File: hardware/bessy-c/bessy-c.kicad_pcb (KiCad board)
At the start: 2 copper layers, 91.5 x 134.5 mm, 55 parts, among them J1 rotary_encoder, J10 fan, J11 auger, J2 probe0, J3 probe1, J4 probe2, J5 PTD, J6 igniter, J7 Display, J8 fire_pit, J9 line_in, K1 1462042-7, K2 1462042-7, K3 1462042-7, Q1 BC847, Q2 SCS-1002K, Q3 BC847, Q4 BC847, U1 ProS3, U2 ADS1115IDGS, U3 MCP96xx01x-x-MX, U4 IRM-10-5, U5 NAU7802SGI

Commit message: Ordered bessy-c pcba rev 1
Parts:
- removed Q2: SCS-1002K, Digikey_SCS_1002K:TRAN_SCS-1002K_SIG
- added C8: 10uF, Capacitor_SMD:C_0805_2012Metric, F.Cu at (94.9, 112.8)
- added D1: 1N4148W, Diode_SMD:D_SOD-123, F.Cu at (124.3, 122.7)
- added D2: 1N4148W, Diode_SMD:D_SOD-123, F.Cu at (116.8, 122.7)
- added D3: 1N4148W, Diode_SMD:D_SOD-123, F.Cu at (106.9, 122.7)
- added D4: BZT52C24, Diode_SMD:D_SOD-123F, F.Cu at (129.4, 122.7)
- added R22: 10k, Resistor_SMD:R_0805_2012Metric, F.Cu at (90.9, 112.8)
- added T1: ZMCT102, kicad-jcl-lib:XFMR_ZMCT102, F.Cu at (93.2, 130.0)
- added U6: ADS1115IDGS, Package_SO:TSSOP-10_3x3mm_P0.5mm, F.Cu at (91.9, 117.6)
- C5, C6, C7: value .1uF -> 0.1uF
- J1: value rotary_encoder -> Conn_01x05; footprint TerminalBlock:TerminalBlock_MaiXu_MX126-5.0-05P_1x05_P5.00mm -> Connector_PinHeader_2.54mm:PinHeader_1x05_P2.54mm_Vertical
- J10: value fan -> DB300V-5.0-2P-BK-S
- J11: value auger -> DB300V-5.0-2P-BK-S
- J2: value probe0 -> DB300V-5.0-2P-BK-S
- J3: value probe1 -> DB300V-5.0-2P-BK-S
- J4: value probe2 -> DB300V-5.0-2P-BK-S
- J5: value PTD -> DB300V-5.0-2P-BK-S
- J6: value igniter -> DB300V-5.0-2P-BK-S
- J7: value Display -> Conn_01x14; footprint Connector_PinHeader_2.54mm:PinHeader_1x15_P2.54mm_Vertical -> Connector_PinHeader_2.54mm:PinHeader_1x14_P2.54mm_Vertical
- J8: value fire_pit -> DB300V-5.0-2P-BK-S
- J9: value line_in -> DB300V-5.0-2P-BK-S
- K1, K2, K3: value 1462042-7 -> G5NB; footprint Digikey_1462042_7_Relay:IM-C_THRU_TEC -> Relay_THT:Relay_SPST_Omron_G5NB
- Q1, Q3, Q4: value BC847 -> MMBT2222A
- R19: value 3k -> 3.3k
- U3: value MCP96xx01x-x-MX -> MCP96L00T-E/MX
- moved J7 71.6 mm to (60.5, 57.1), turned to 0 degrees
- moved R3 33.5 mm to (93.6, 50.0)
- moved J1 33.4 mm to (111.5, 46.0), turned to -90 degrees
- moved R1 33.1 mm to (97.8, 55.0), turned to -90 degrees
- moved C2 32.2 mm to (93.0, 55.0)
- moved R2 30.3 mm to (97.8, 59.0), turned to -90 degrees
- moved C1 29.5 mm to (93.0, 59.0)
- moved R4 27.4 mm to (110.6, 63.2), turned to 180 degrees
- moved J2 25.0 mm to (126.0, 60.2)
- moved J3 25.0 mm to (126.0, 74.2)
- moved J4 25.0 mm to (126.0, 88.2)
- moved J5 25.0 mm to (126.0, 101.7)
- moved J8 25.0 mm to (126.0, 115.2)
- moved U2 24.9 mm to (106.2, 68.1)
- moved R7 23.2 mm to (106.3, 63.2), turned to 0 degrees
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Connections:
- Q1 pad 3: Net-(Q1-C) -> Net-(D3-A)
- Q3 pad 3: Net-(Q3-C) -> Net-(D2-A)
- Q4 pad 3: Net-(Q4-C) -> Net-(D1-A)
- R10 pad 1: GND -> Net-(U6-AIN3)
- R10 pad 2: /igniter_current -> Net-(U6-AIN2)
- U1 pad 16: /tft_cs -> unconnected-(U1-IO13-Pad16)
- U1 pad 17: /tft_dc -> unconnected-(U1-IO12-Pad17)
- U1 pad 18: /IO42 -> /auger
- U1 pad 19: /auger -> /fan
- U1 pad 20: /fan -> /igniter
- U1 pad 21: /igniter -> /tft_cs
- U1 pad 22: /IO38 -> /tft_rst
- U1 pad 23: /IO44 -> /tft_dc
- U2 pad 7: /igniter_current -> unconnected-(U2-AIN3-Pad7)
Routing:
- net /igniter_current: track 69.8 -> 0.00 mm
- net /tft_dc: track 61.0 -> 8.12 mm, vias 2 -> 0
- net +3.3V: track 237.6 -> 187.9 mm, vias 4 -> 10
- net /tft_cs: track 57.3 -> 8.51 mm, vias 2 -> 0
- net /enc_b: track 52.6 -> 12.0 mm
- net Net-(J5-Pin_1): track 53.6 -> 14.1 mm, vias 1 -> 0
- net /spi_miso: track 65.8 -> 28.6 mm, vias 1 -> 0
- net Net-(U5-AVDD/LDO): track 22.7 -> 59.0 mm
- net /enc_a: track 47.3 -> 12.6 mm
- net +5V: track 155.5 -> 189.5 mm
- net Net-(J8-Pin_1): track 44.1 -> 11.7 mm
- net /spi_clk: track 64.2 -> 32.5 mm, vias 2 -> 0
- net /spi_mosi: track 60.5 -> 29.2 mm, vias 2 -> 0
- net Net-(J5-Pin_2): track 37.4 -> 8.92 mm, vias 1 -> 0
- net Net-(Q1-C): track 28.5 -> 0.00 mm, vias 1 -> 0
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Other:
- board size 91.5 x 134.5 mm -> 77.5 x 118 mm
- board text added: "JLCJLCJLCJLC"
- board text removed: "Main Sheet"

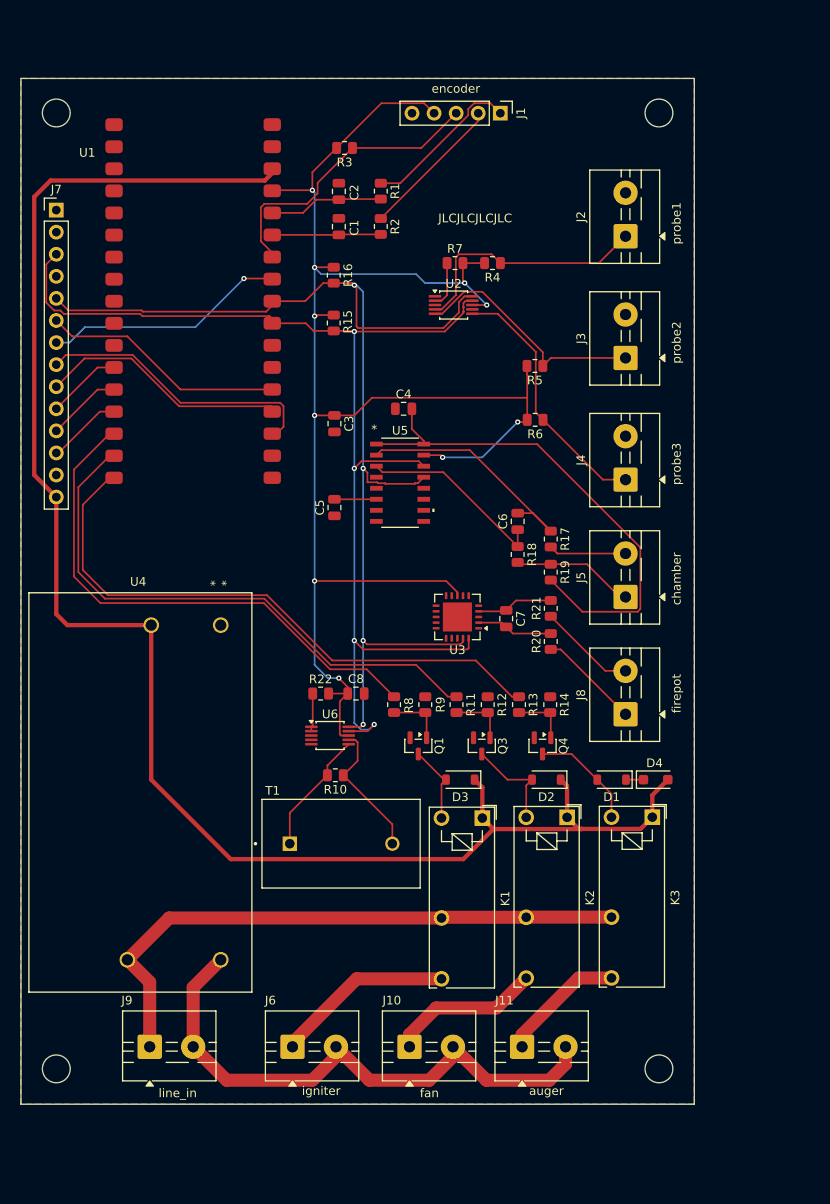
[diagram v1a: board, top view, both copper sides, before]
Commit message: r2 of board with bodge wires fixed
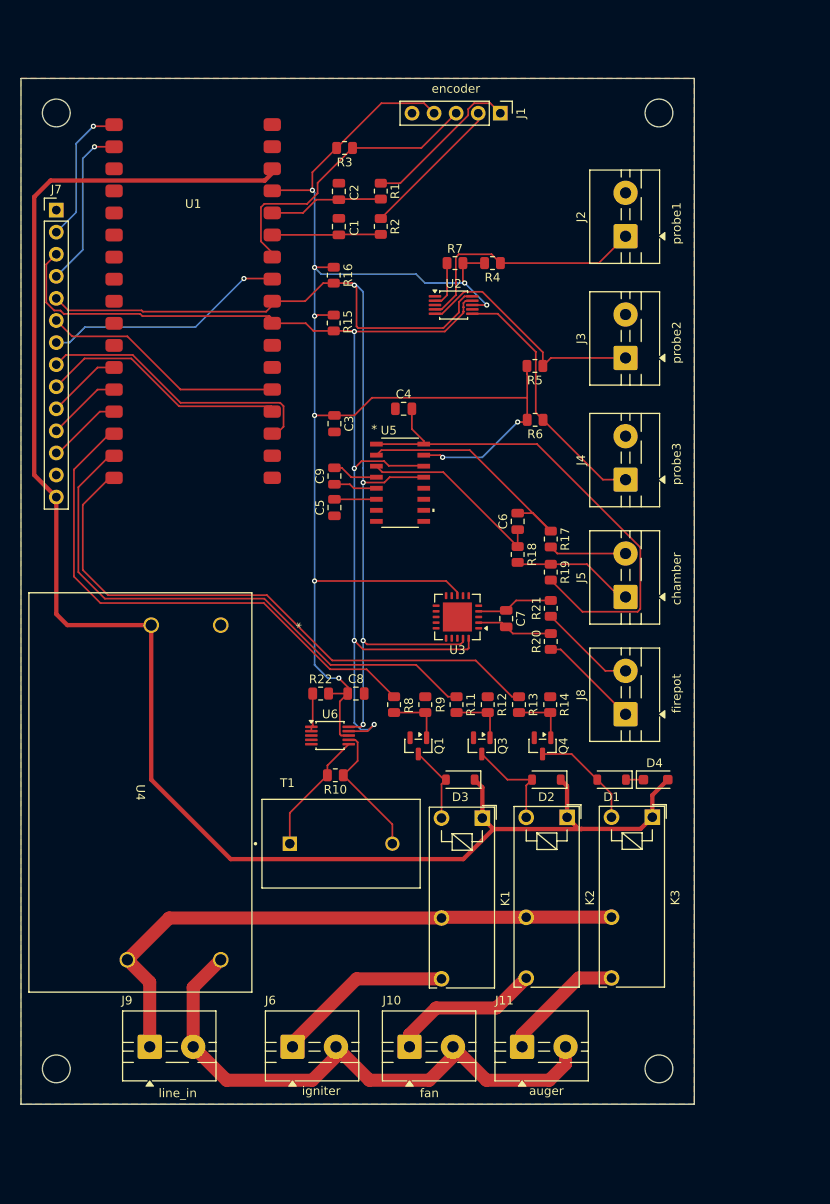
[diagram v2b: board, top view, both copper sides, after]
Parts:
- added C9: 0.1uF, Capacitor_SMD:C_0805_2012Metric, F.Cu at (92.5, 87.7)
- T1: footprint kicad-jcl-lib:XFMR_ZMCT102 -> DigiKey-jcl:XFMR_ZMCT102
- U1: footprint kicad-jcl-lib:ProS3_SMD -> DigiKey-jcl:ProS3_SMD
- U4: footprint Digikey_IRM_10_5:IRM-10_MWU -> DigiKey-jcl:IRM-10_MWU
- U5: footprint Digikey_NAU7802SGI:SOI16_NAU7802SGI_NUV -> DigiKey-jcl:SOI16_NAU7802SGI_NUV
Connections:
- J5 pad 2: Net-(J5-Pin_2) -> GND
- R17 pad 2: Net-(J5-Pin_2) -> GND
- U1 pad 33: /IO37 -> /ctc_rst
- U1 pad 34: /IO35 -> /ctc_int
- U5 pad 4: unconnected-(U5-VIN2N-Pad4) -> Net-(U5-VIN2N)
- U5 pad 5: unconnected-(U5-VIN2P-Pad5) -> Net-(U5-VIN2P)
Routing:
- net /ctc_rst: track 0.00 -> 18.5 mm, vias 0 -> 1
- net /ctc_int: track 0.00 -> 15.9 mm, vias 0 -> 1
- net Net-(J5-Pin_2): track 8.92 -> 0.00 mm
- net GND: track 0.00 -> 8.92 mm
- net Net-(U5-VIN2N): track 0.00 -> 5.28 mm
- net Net-(U5-VIN2P): track 0.00 -> 5.02 mm
- net /i2c_scl: track 130.7 -> 129.2 mm
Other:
- board text removed: "JLCJLCJLCJLC"
